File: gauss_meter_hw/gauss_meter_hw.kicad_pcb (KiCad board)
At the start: 2 copper layers, 15 parts, among them J1 Conn_01x04, U1 INA326

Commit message: initial PCB design
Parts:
- added J2: 128x64 - SSH1106, Connector_PinSocket_2.54mm:PinSocket_1x04_P2.54mm_Vertical, F.Cu at (121.7, 89.3)
- added REF**: KiCad-Logo2_8mm_SilkScreen, Symbol:KiCad-Logo2_8mm_SilkScreen, F.Cu at (141.9, 84.1)
- added REF**: OSHW-Logo2_7.3x6mm_SilkScreen, Symbol:OSHW-Logo2_7.3x6mm_SilkScreen, F.Cu at (141.5, 92.5)
- moved C5 39.8 mm to (165.4, 82.3), turned to 180 degrees
- moved R2 37.9 mm to (177.4, 94.7)
- moved RV1 35.2 mm to (171.2, 93.6), turned to 270 degrees
- moved R4 35.0 mm to (177.3, 85.3)
- moved R5 32.2 mm to (169.8, 78.0), turned to 270 degrees
- moved C4 31.3 mm to (165.4, 80.0), turned to 180 degrees
- moved C1 28.1 mm to (177.3, 83.0)
- moved C3 27.7 mm to (172.1, 78.0), turned to 270 degrees
- moved RV2 24.0 mm to (164.8, 86.4), turned to 270 degrees
- moved R1 23.8 mm to (177.3, 80.8)
- moved C2 22.4 mm to (177.3, 87.7)
- moved U1 21.8 mm to (170.8, 86.0), turned to 90 degrees
- moved J1 18.7 mm to (181.5, 81.5)
- moved R3 11.1 mm to (177.3, 89.9), turned to 180 degrees
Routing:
- net +5V: track 0.00 -> 140.3 mm
- net Net-(A1-Pad14): track 0.00 -> 72.3 mm
- net Net-(A1-Pad13): track 0.00 -> 64.7 mm
- net Net-(C1-Pad1): track 0.00 -> 20.1 mm
- net Net-(A1-Pad9): track 0.00 -> 16.9 mm
- net Net-(RV2-Pad1): track 0.00 -> 9.76 mm
- net Net-(C2-Pad1): track 0.00 -> 8.80 mm
- net Net-(RV1-Pad2): track 0.00 -> 6.08 mm
- net Net-(R5-Pad2): track 0.00 -> 4.59 mm
- net Net-(RV2-Pad3): track 0.00 -> 4.29 mm
- net Net-(R3-Pad2): track 0.00 -> 3.63 mm
- net Net-(R2-Pad1): track 0.00 -> 2.70 mm
- net GND: vias 0 -> 4
- added copper zone on B.Cu, net GND
- added copper zone on F.Cu, net GND
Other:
- board outline added: 69 x 53.9 mm
- board text added: "Gauss Meter Arduino Shield"
- board text added: "Stefan Andrei Chelariu (c)2019"

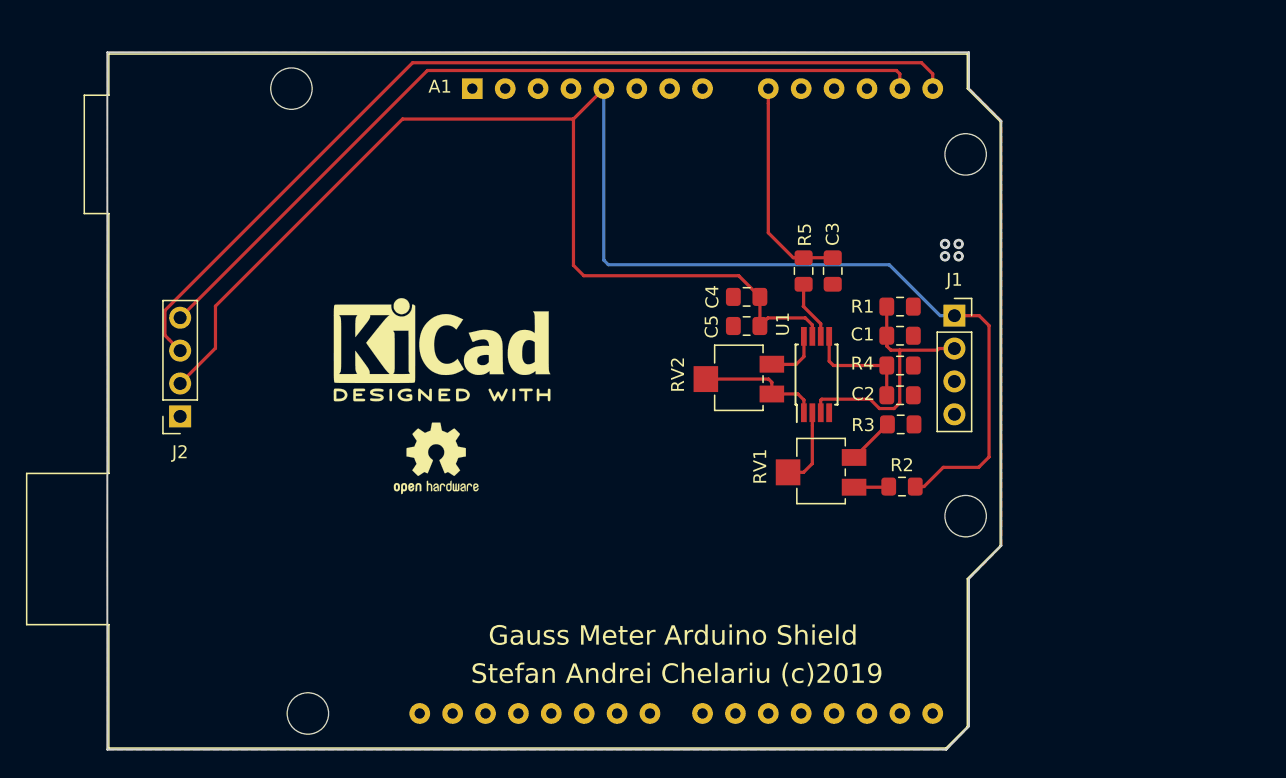
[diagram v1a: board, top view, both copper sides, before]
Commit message: revised for correct board orientation
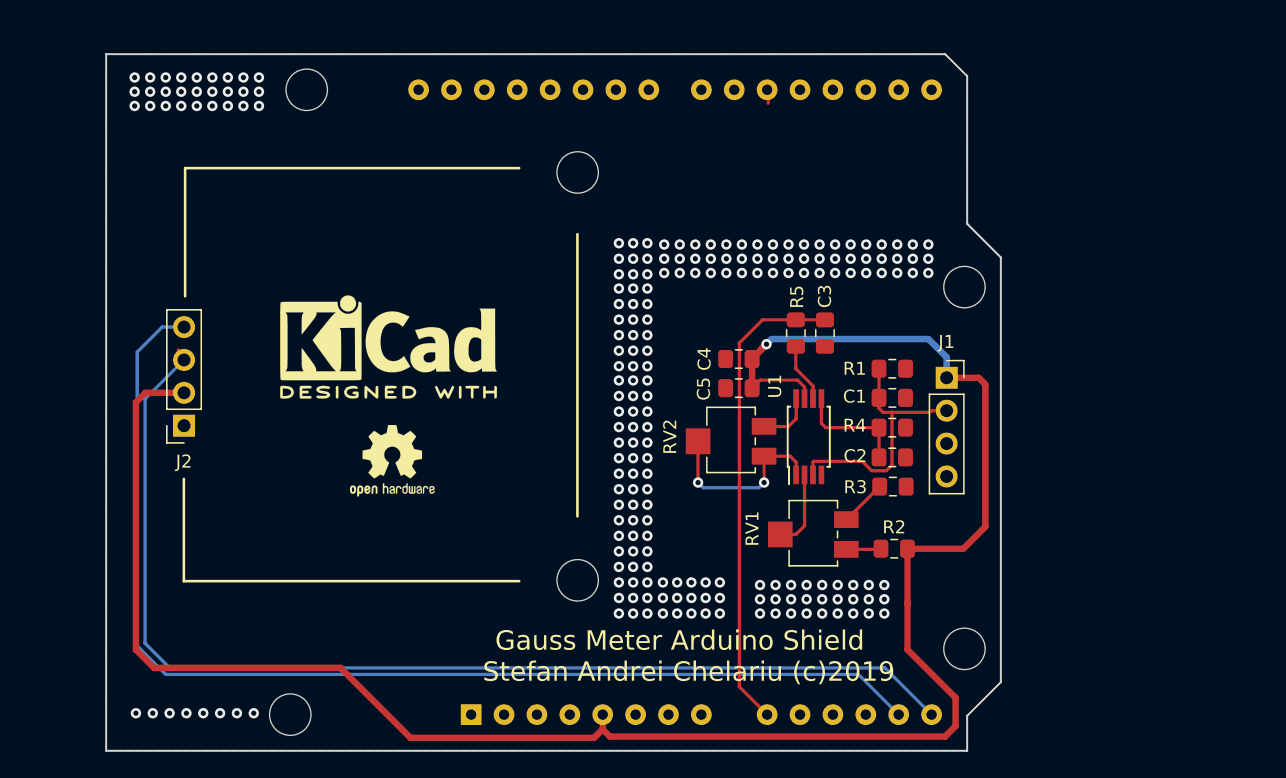
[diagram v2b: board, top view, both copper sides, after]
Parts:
- added REF**: MountingHole_3.2mm_M3, MountingHole:MountingHole_3.2mm_M3, F.Cu at (152.4, 70.4)
- added REF**: MountingHole_3.2mm_M3, MountingHole:MountingHole_3.2mm_M3, F.Cu at (152.4, 101.9)
- A1: moved to B.Cu
- moved A1 48.4 mm to (144.2, 112.3)
- moved R4 4.84 mm to (176.7, 90.2)
- moved RV1 4.84 mm to (170.6, 98.4)
- moved C1 4.84 mm to (176.7, 87.8)
- moved C2 4.84 mm to (176.7, 92.5)
- moved R1 4.84 mm to (176.7, 85.6)
- moved C3 4.84 mm to (171.5, 82.8)
- moved C4 4.84 mm to (164.8, 84.8)
- moved C5 4.84 mm to (164.8, 87.1)
- moved J1 4.84 mm to (180.9, 86.3)
- moved R2 4.84 mm to (176.8, 99.5)
- moved R3 4.84 mm to (176.8, 94.7)
- moved R5 4.84 mm to (169.2, 82.8)
- moved RV2 4.84 mm to (164.2, 91.2)
- moved U1 4.84 mm to (170.2, 90.8)
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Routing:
- net Net-(A1-Pad13): track 64.7 -> 88.1 mm
- net Net-(A1-Pad9): track 16.9 -> 36.9 mm
- net Net-(A1-Pad14): track 72.3 -> 87.4 mm
- net +5V: track 140.3 -> 154.2 mm, vias 0 -> 1
- net Net-(RV2-Pad1): track 9.76 -> 14.3 mm, vias 0 -> 2
- net Net-(A1-Pad20): track 0.00 -> 1.13 mm
- net GND: vias 4 -> 206
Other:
- board size 69 x 53.9 mm -> 69.1 x 53.8 mm
- net class V added: clearance 0.2, trace_width 0.5, via_dia 0.8, via_drill 0.4
